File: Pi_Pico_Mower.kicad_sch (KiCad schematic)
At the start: 25 parts, among them U1 Pico

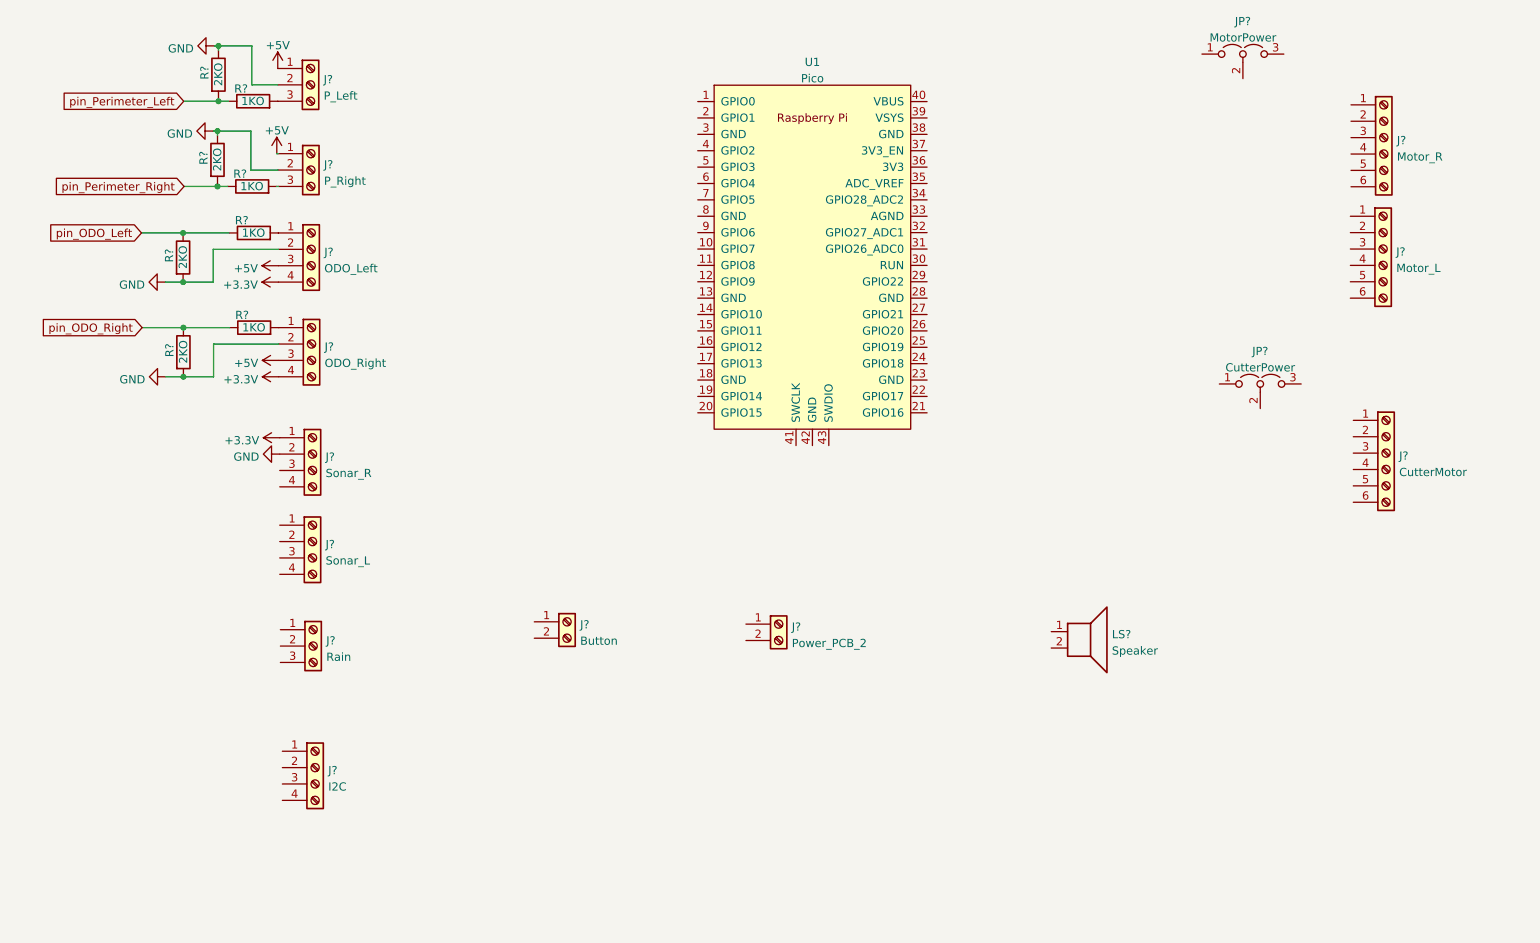
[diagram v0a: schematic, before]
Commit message: Add new Pins
New Pins, Power Supply and Gy-271
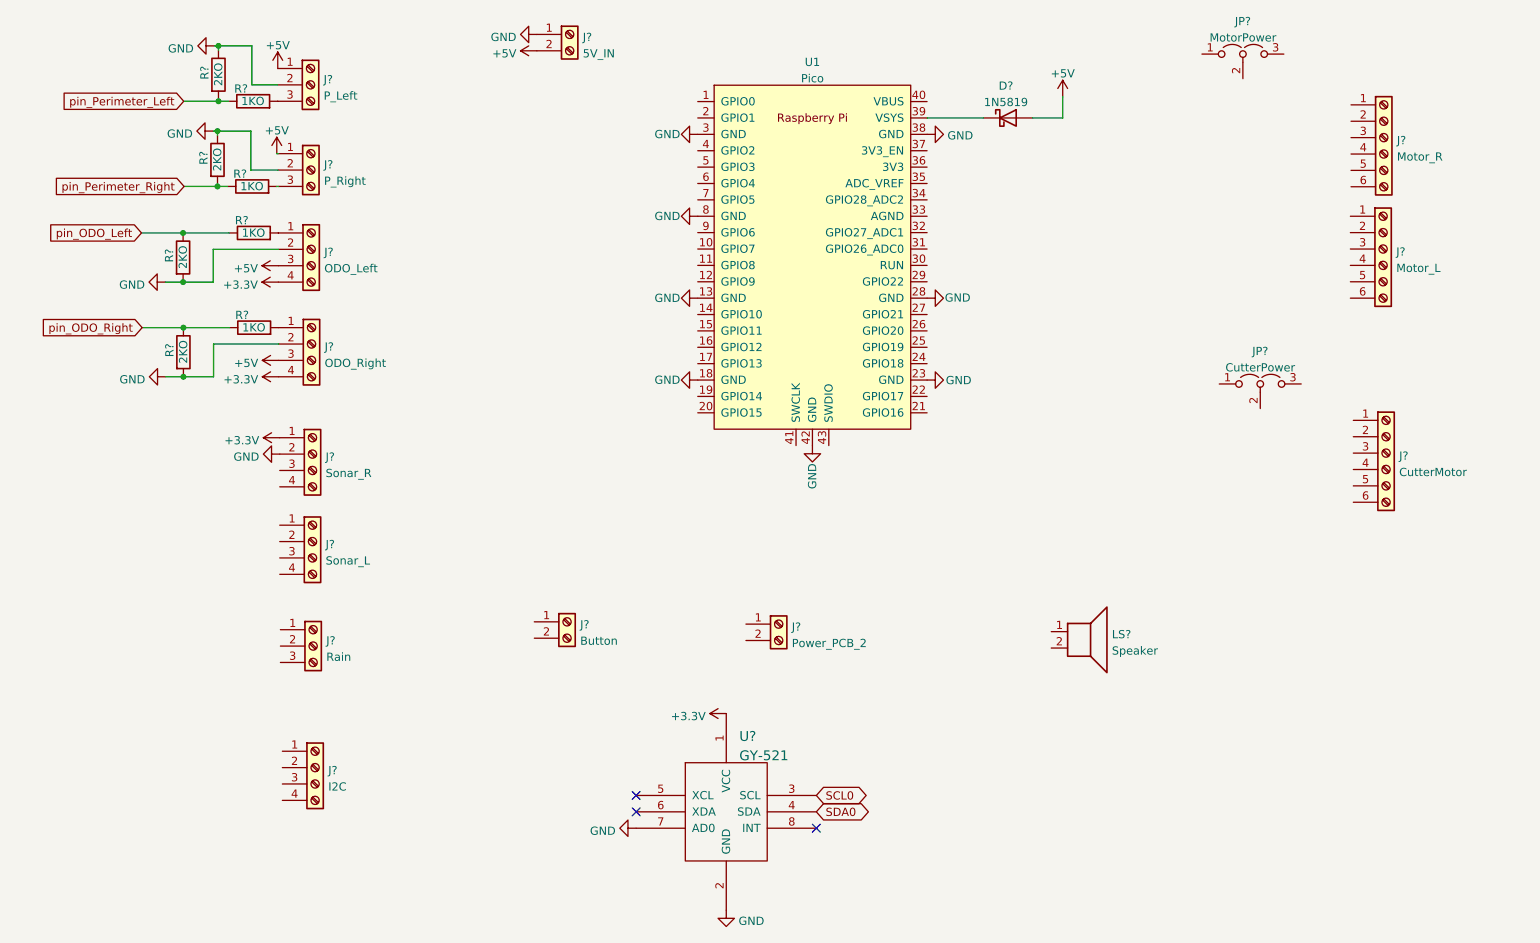
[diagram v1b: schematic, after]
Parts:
- added D?: 1N5819, Diode_THT:D_DO-41_SOD81_P10.16mm_Horizontal, symbol Diode:1N5819
- added J?: 5V_IN, symbol Connector:Screw_Terminal_01x02
- added U?: GY-521, symbol gy-521:GY-521
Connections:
- net +3V3: now also U?.1 (VCC)
- net +5V: now also D?.2 (A), J?.2 (Pin_2)
- net GND: now also U1.13 (GND), U1.18 (GND), U1.23 (GND), U1.28 (GND), U1.3 (GND), U1.38 (GND), U1.42 (GND), U1.8 (GND), J?.1 (Pin_1), U?.2 (GND), U?.7 (AD0)
- net at U1.39 (VSYS): now also D?.1 (K)
- new net SCL0: U?.3 (SCL)
- new net SDA0: U?.4 (SDA)
- no-connect marks 0 -> 3

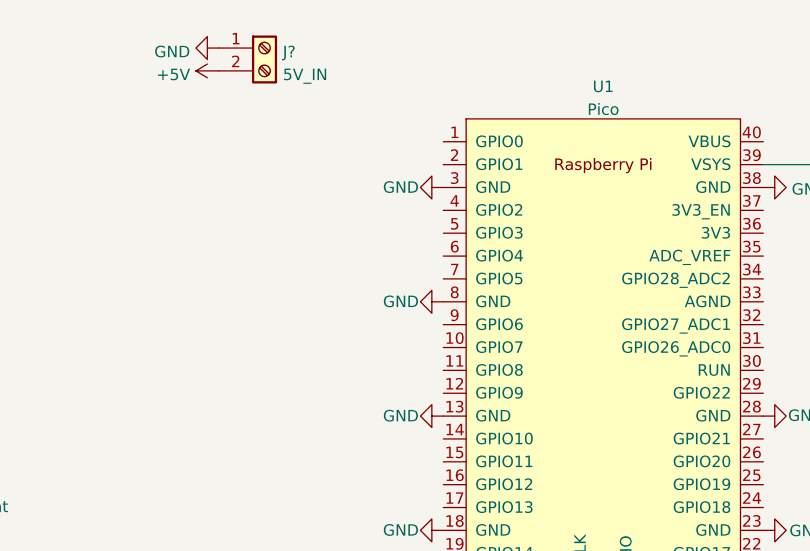
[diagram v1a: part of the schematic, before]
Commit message: Add SCL SDA
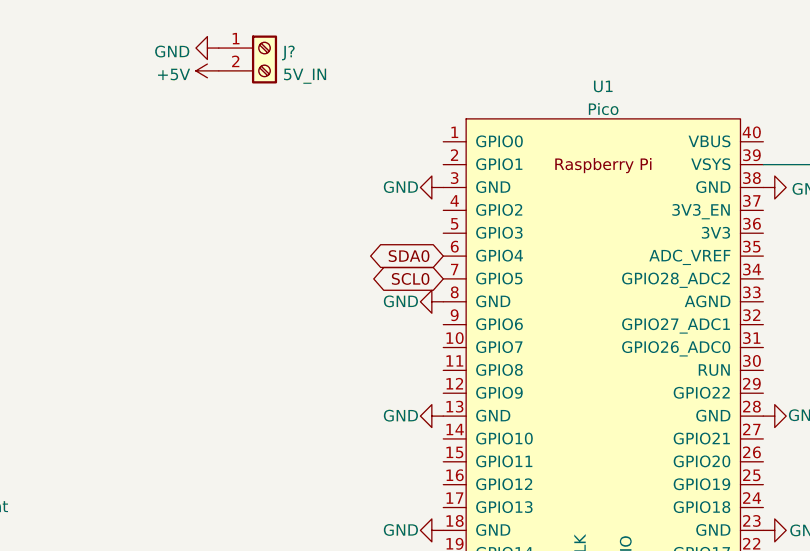
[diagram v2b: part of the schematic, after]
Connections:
- net SCL0: now also U1.7 (GPIO5)
- net SDA0: now also U1.6 (GPIO4)
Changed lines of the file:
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@@
+    )
+  )
+  (global_label "SDA0" (shape bidirectional) (at 119.634 38.4556 180) (fields_autoplaced)
+    (effects (font (size 1.27 1.27)) (justify right))
+    (property "Intersheet References" "${INTERSHEET_REFS}" (id 0) (at 112.4433 38.3762 0)
+      (effects (font (size 1.27 1.27)) (justify right) hide)
     )
   )
@@
       (effects (font (size 1.27 1.27)) (justify right) hide)
     )
+  )
+  (global_label "SCL0" (shape bidirectional) (at 119.634 40.9956 180) (fields_autoplaced)
+    (effects (font (size 1.27 1.27)) (justify right))
+    (property "Intersheet References" "${INTERSHEET_REFS}" (id 0) (at 112.5038 40.9162 0)
+      (effects (font (size 1.27 1.27)) (justify right) hide)
+    )

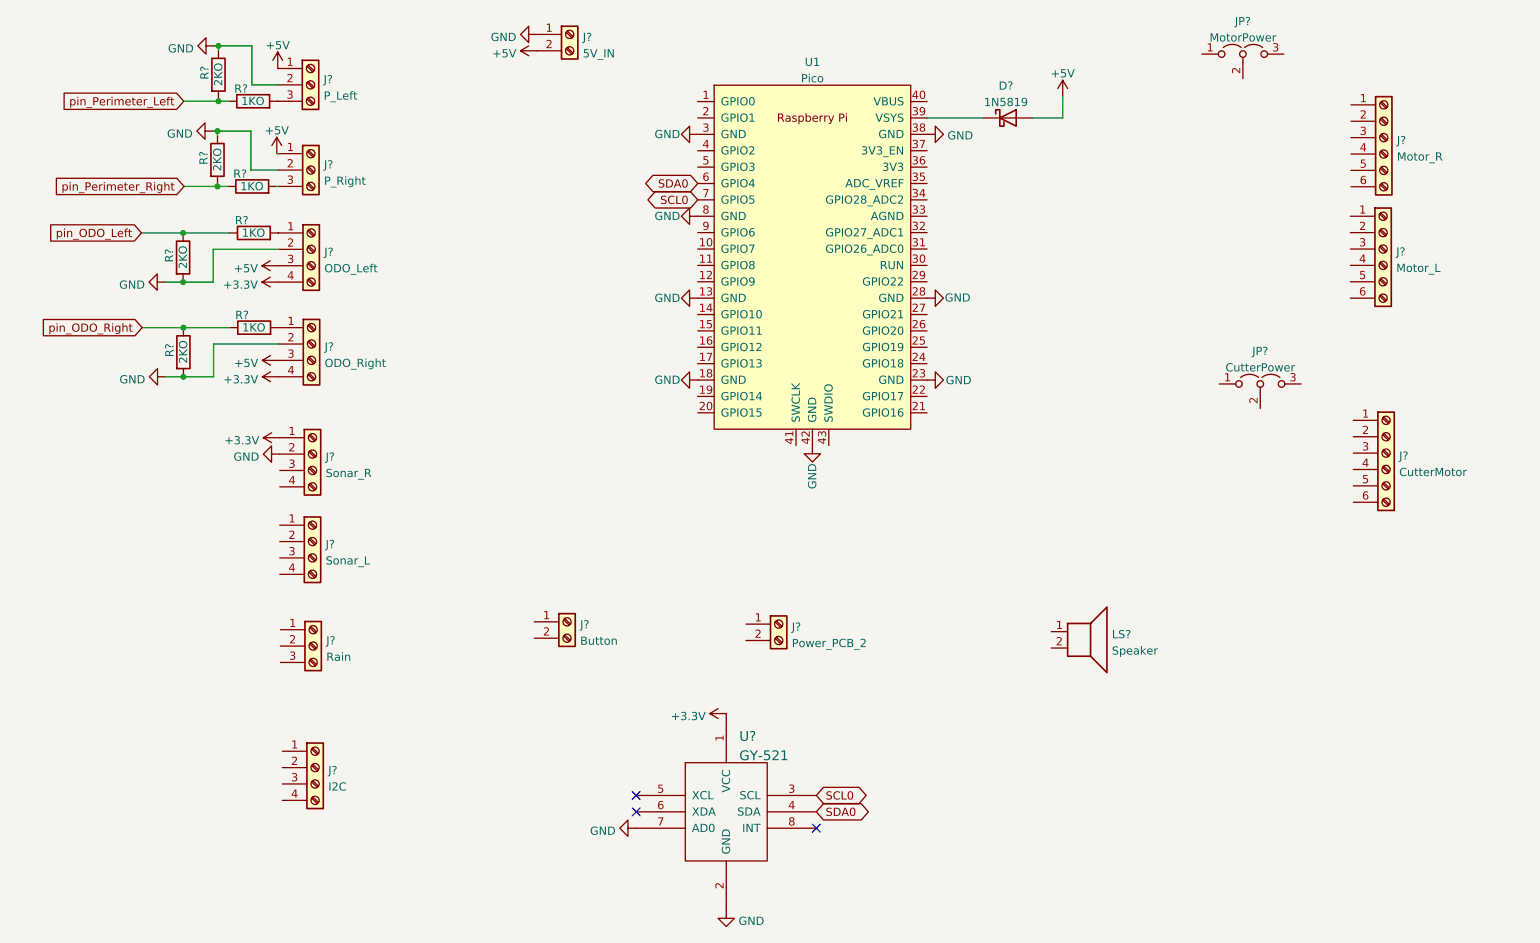
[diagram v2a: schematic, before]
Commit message: Add Pin Description
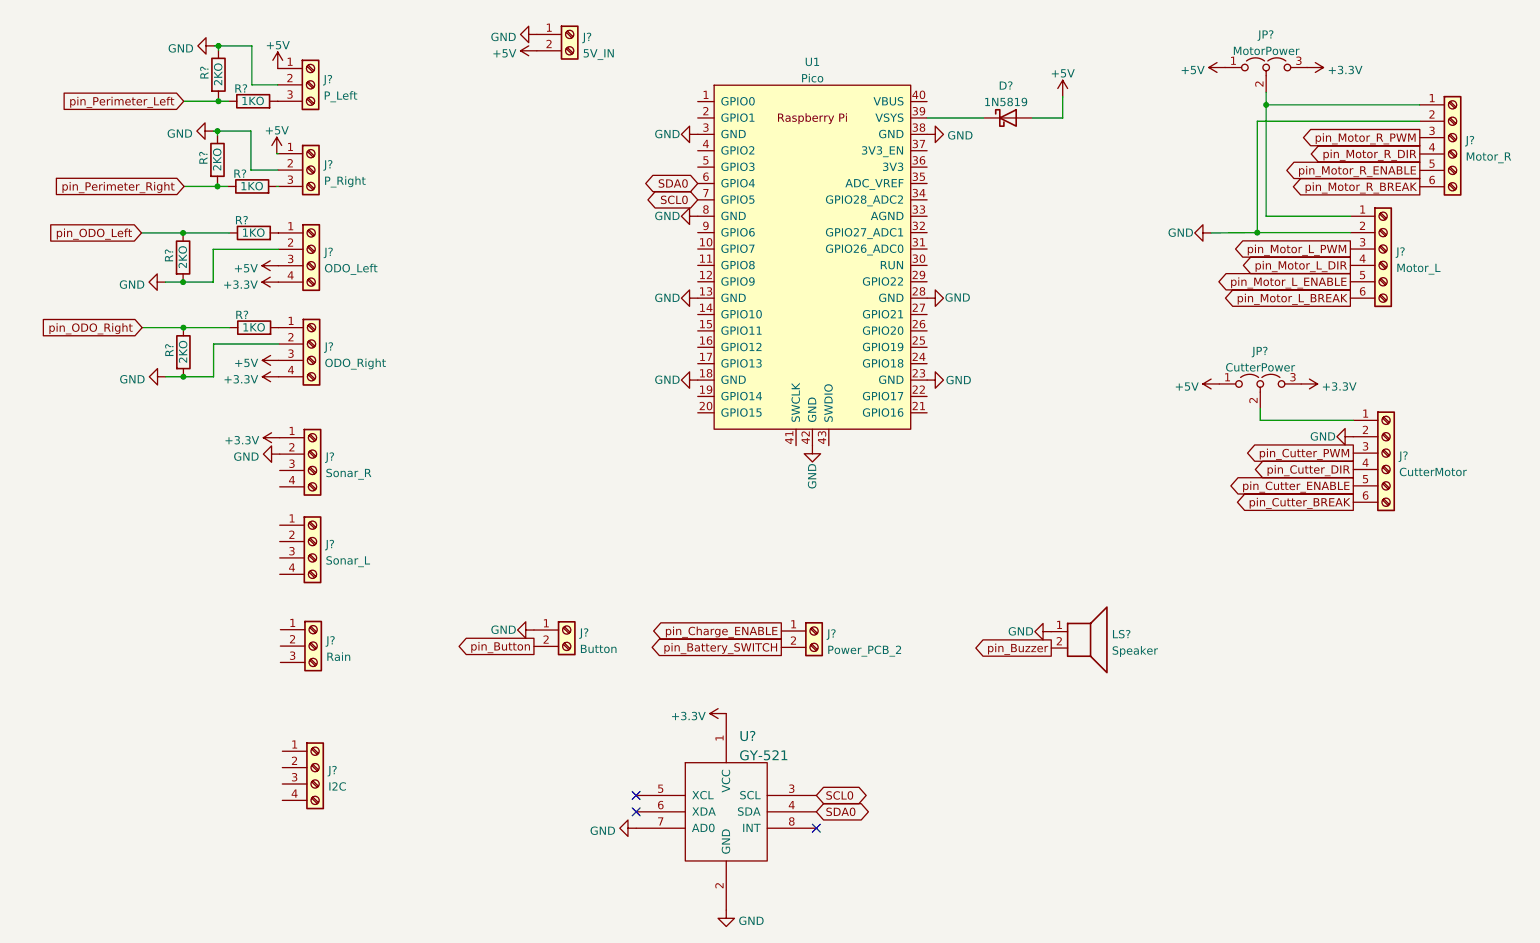
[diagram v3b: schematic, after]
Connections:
- net +3V3: now also JP?.3 (B), JP?.3 (B)
- net +5V: now also JP?.1 (A), JP?.1 (A)
- net GND: now also J?.1 (Pin_1), J?.2 (Pin_2), J?.2 (Pin_2), J?.2 (Pin_2), LS?.1
- net pin_Charge_ENABLE: now reaches J?.1 (Pin_1)
- net pin_Battery_SWITCH: now reaches J?.2 (Pin_2)
- net at J?.1 (Pin_1): now also J?.1 (Pin_1), JP?.2 (C)
- net pin_Motor_L_PWM: now reaches J?.3 (Pin_3)
- net pin_Motor_L_DIR: now reaches J?.4 (Pin_4)
- net pin_Motor_L_ENABLE: now reaches J?.5 (Pin_5)
- net pin_Motor_L_BREAK: now reaches J?.6 (Pin_6)
- net pin_Button: now reaches J?.2 (Pin_2)
- net pin_Motor_R_PWM: now reaches J?.3 (Pin_3)
- net pin_Motor_R_DIR: now reaches J?.4 (Pin_4)
- net pin_Motor_R_ENABLE: now reaches J?.5 (Pin_5)
- net pin_Motor_R_BREAK: now reaches J?.6 (Pin_6)
- net pin_Buzzer: now reaches LS?.2
- net at J?.1 (Pin_1): now also JP?.2 (C)
- net pin_Cutter_PWM: now reaches J?.3 (Pin_3)
- net pin_Cutter_DIR: now reaches J?.4 (Pin_4)
- net pin_Cutter_ENABLE: now reaches J?.5 (Pin_5)
- net pin_Cutter_BREAK: now reaches J?.6 (Pin_6)
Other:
- moved on the sheet: J?, JP?

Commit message: Add Pins to Pico
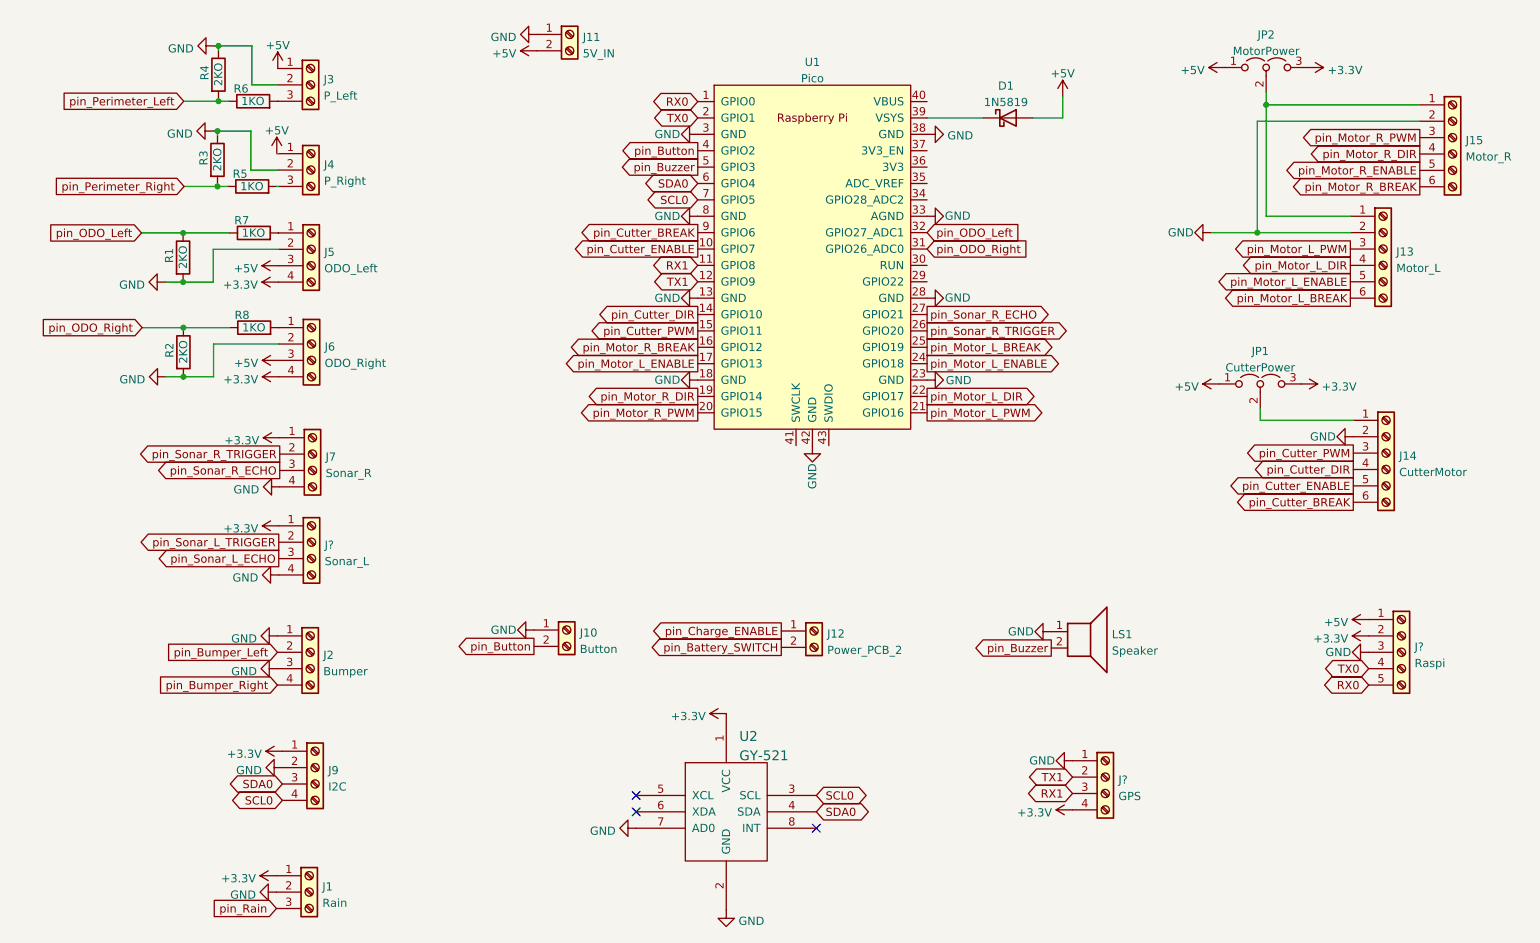
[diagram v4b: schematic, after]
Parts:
- removed J?: Sonar_L, symbol Connector:Screw_Terminal_01x04
- added J2: Bumper, symbol Connector:Screw_Terminal_01x04
- added J?: Sonar_L, symbol Connector:Screw_Terminal_01x04
- added J?: GPS, symbol Connector:Screw_Terminal_01x04
- added J?: Raspi, symbol Connector:Screw_Terminal_01x05
- gave numbers to parts that had none: 26
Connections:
- net +3V3: now also J1.1 (Pin_1), J9.1 (Pin_1), J?.1 (Pin_1), J?.2 (Pin_2), J?.4 (Pin_4)
- net +5V: now also J?.1 (Pin_1)
- net GND: now also J1.2 (Pin_2), J7.4 (Pin_4), J9.2 (Pin_2), U1.33 (AGND), J2.1 (Pin_1), J2.3 (Pin_3), J?.1 (Pin_1), J?.3 (Pin_3), J?.4 (Pin_4); no longer J7.2 (Pin_2)
- net SCL0: now also J9.4 (Pin_4)
- net SDA0: now also J9.3 (Pin_3)
- net pin_Button: now also U1.4 (GPIO2)
- net pin_Buzzer: now also U1.5 (GPIO3)
- net pin_Cutter_BREAK: now also U1.9 (GPIO6)
- net pin_Cutter_DIR: now also U1.14 (GPIO10)
- net pin_Cutter_ENABLE: now also U1.10 (GPIO7)
- net pin_Cutter_PWM: now also U1.15 (GPIO11)
- net pin_Motor_L_BREAK: now also U1.25 (GPIO19)
- net pin_Motor_L_DIR: now also U1.22 (GPIO17)
- net pin_Motor_L_ENABLE: now also U1.17 (GPIO13), U1.24 (GPIO18)
- net pin_Motor_L_PWM: now also U1.21 (GPIO16)
- net pin_Motor_R_BREAK: now also U1.16 (GPIO12)
- net pin_Motor_R_DIR: now also U1.19 (GPIO14)
- net pin_Motor_R_PWM: now also U1.20 (GPIO15)
- net pin_ODO_Left: now also U1.32 (GPIO27_ADC1)
- net pin_ODO_Right: now also U1.31 (GPIO26_ADC0)
- net RX0: now reaches U1.1 (GPIO0)
- net RX0: now also J?.5 (Pin_5)
- net RX1: now reaches U1.11 (GPIO8)
- net RX1: now also J?.3 (Pin_3)
- net TX1: now reaches U1.12 (GPIO9)
- net TX1: now also J?.2 (Pin_2)
- net TX0: now reaches U1.2 (GPIO1)
- net TX0: now also J?.4 (Pin_4)
- net pin_Sonar_R_TRIGGER: now reaches U1.26 (GPIO20)
- net pin_Sonar_R_TRIGGER: now also J7.2 (Pin_2)
- net pin_Sonar_R_ECHO: now reaches U1.27 (GPIO21)
- net pin_Sonar_R_ECHO: now also J7.3 (Pin_3)
- net pin_Rain: now reaches J1.3 (Pin_3)
- new net pin_Bumper_Left: J2.2 (Pin_2)
- new net pin_Bumper_Right: J2.4 (Pin_4)
- new net pin_Sonar_L_ECHO: J?.3 (Pin_3)
- new net pin_Sonar_L_TRIGGER: J?.2 (Pin_2)
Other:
- moved on the sheet: J1
